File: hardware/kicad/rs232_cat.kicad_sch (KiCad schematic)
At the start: 7 parts, among them U4 MAX202EESE+T

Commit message: fix: repair schematic connectivity, real MAX3421E pinout, footprint assignment
- Root sheet pins were placed outside the sheet boxes, so no cross-sheet
  net (IO5->CI-V, USB D+/D-, SPI, VBUS_5V, 5V_HOST) was actually connected.
  Rebuilt pins on the sheet borders with wire stubs + labels.
- MCU: SW1/SW2 pin 2 carried both GND and EN/BOOT0 (short to ground);
  GND moved to pin 1. Unused ESP32 GPIOs marked no-connect.
- USB_Host rebuilt around the real MAX3421E TQFN-32 pinout (datasheet
  19-3953): 33 ohm D+/D- series resistors, 1uF VCC/VBCOMP, 0.1uF VL.
- J1 now AudioJack3 (T/R/S) with CUI SJ1-3523N footprint; Q1 is a real
  2N7000 (TO-92).
- PWR_FLAGs added; ERC (raw kicad-cli) has 0 errors.
- Board outline 65x45 mm, 54 footprints assigned and written to symbol
  Footprint fields, netlist applied. Placement is a rough grid only; no
  routing yet.
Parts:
- C4, C5, C6, C7, C8: footprint (none) -> Capacitor_SMD:C_0603_1608Metric
- DSUB1: footprint (none) -> Connector_Dsub:DSUB-9_Socket_Horizontal_P2.77x2.54mm_EdgePinOffset9.40mm
- U4: footprint (none) -> Package_SO:SOIC-16_4.55x10.3mm_P1.27mm
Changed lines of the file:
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@@
 			)
 		)
-		(property "Footprint" ""
+		(property "Footprint" "Connector_Dsub:DSUB-9_Socket_Horizontal_P2.77x2.54mm_EdgePinOffset9.40mm"
 			(at 75 110 0)
 			(effects
@@
 			)
 		)
-		(property "Footprint" ""
+		(property "Footprint" "Package_SO:SOIC-16_4.55x10.3mm_P1.27mm"
 			(at 40 110 0)
 			(effects
@@
 			)
 		)
-		(property "Footprint" ""
+		(property "Footprint" "Capacitor_SMD:C_0603_1608Metric"
 			(at 10 91 0)
 			(effects
@@
 			)
 		)
-		(property "Footprint" ""
+		(property "Footprint" "Capacitor_SMD:C_0603_1608Metric"
 			(at 70 91 0)
 			(effects
@@
 			)
 		)
-		(property "Footprint" ""
+		(property "Footprint" "Capacitor_SMD:C_0603_1608Metric"
 			(at 70 100 0)
 			(effects
@@
 			)
 		)
-		(property "Footprint" ""
+		(property "Footprint" "Capacitor_SMD:C_0603_1608Metric"
 			(at 70 108 0)
 			(effects
@@
 			)
 		)
-		(property "Footprint" ""
+		(property "Footprint" "Capacitor_SMD:C_0603_1608Metric"
 			(at 30 82 0)
 			(effects

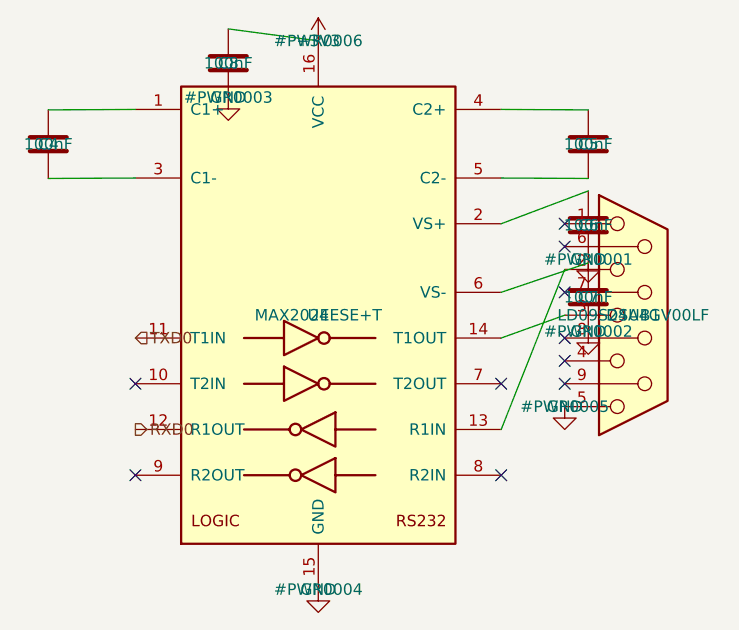
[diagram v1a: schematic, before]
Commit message: fix: datasheet audit - correct charger pinout, LDO for 3V3, DW01A/FS8205A, MAX3232, CI-V RX
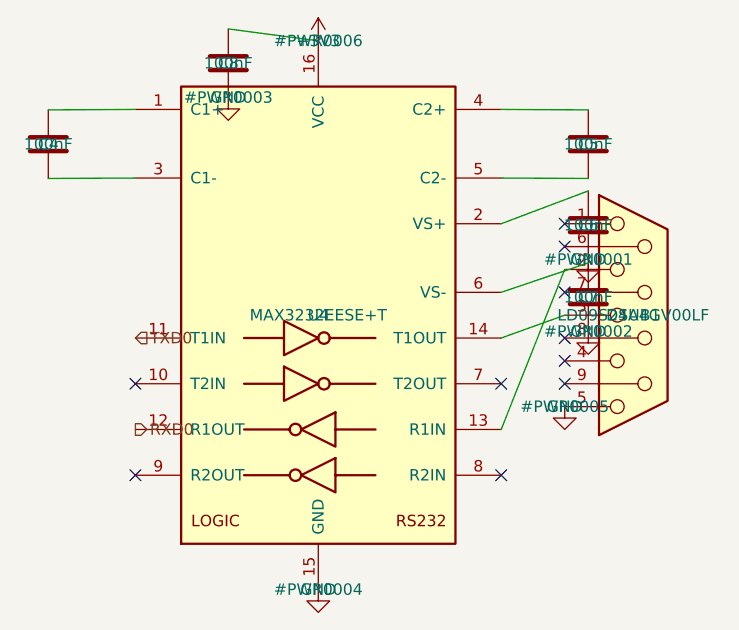
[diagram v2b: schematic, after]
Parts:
- U4: value MAX202EESE+T -> MAX3232EESE+T; footprint Package_SO:SOIC-16_4.55x10.3mm_P1.27mm -> Package_SO:SOIC-16_3.9x9.9mm_P1.27mm
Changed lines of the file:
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@@
 			)
 		)
-		(property "Value" "MAX202EESE+T"
+		(property "Value" "MAX3232EESE+T"
 			(at 40 110 0)
 			(effects
@@
 			)
 		)
-		(property "Footprint" "Package_SO:SOIC-16_4.55x10.3mm_P1.27mm"
+		(property "Footprint" "Package_SO:SOIC-16_3.9x9.9mm_P1.27mm"
 			(at 40 110 0)
 			(effects
